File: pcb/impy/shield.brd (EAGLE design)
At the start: 137 x 101 mm, 120 parts, among them J1 USB-2410-06, J2 SI-60062-F, J3 5V, U1 AD5933YRS, U10 LTC3406AB, U11 23LCV1024-I/SN, U12 MIC2009A-1YM6, U13 ADG725BSU, U14 ADG725BSU, U15 ADG819BRT, U2 ADG704BRM, U3 AD8656ARZ, U4 M24C08WMN, U5 ADG706BRU, U6 DP83848I, U7 MIC2009A-1YM6, U8 AT25DF081A-SS, U9 SST25VF080B-80-4I-S2

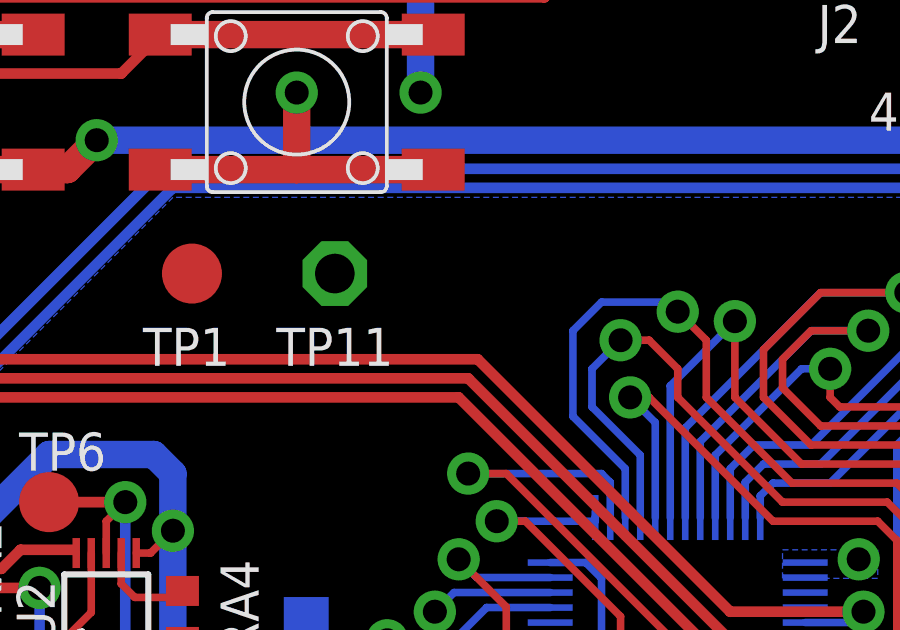
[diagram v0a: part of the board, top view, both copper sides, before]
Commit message: * pcb/impy: (shield.brd) Move GND test pin away from reset button.
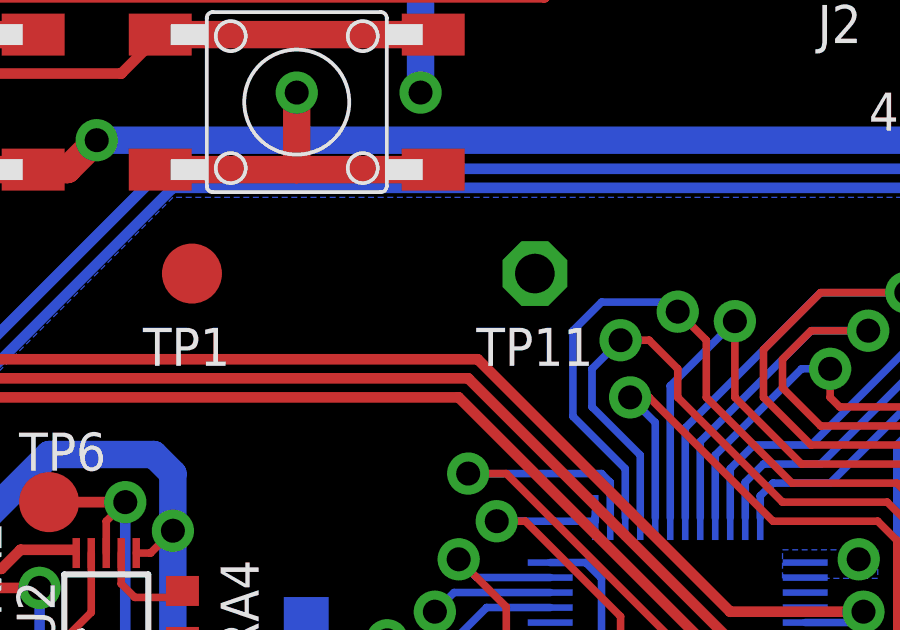
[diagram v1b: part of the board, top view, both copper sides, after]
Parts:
- moved TP11 6.67 mm to (68.6, 67.0)
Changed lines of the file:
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@@
 <attribute name="VALUE" x="47.498" y="52.0065" size="0.0254" layer="27"/>
 </element>
-<element name="TP11" library="testpad" package="P1-13" value="TPPAD1-13" x="61.9125" y="66.9925" smashed="yes">
-<attribute name="TP_SIGNAL_NAME" value="AGND" x="60.0075" y="64.135" size="1" layer="37"/>
-<attribute name="NAME" x="59.96" y="63.915" size="1.27" layer="25"/>
-<attribute name="VALUE" x="61.1505" y="65.9765" size="0.0254" layer="27"/>
+<element name="TP11" library="testpad" package="P1-13" value="TPPAD1-13" x="68.58" y="66.9925" smashed="yes">
+<attribute name="TP_SIGNAL_NAME" value="AGND" x="66.675" y="64.135" size="1" layer="37"/>
+<attribute name="NAME" x="66.6275" y="63.915" size="1.27" layer="25"/>
+<attribute name="VALUE" x="67.818" y="65.9765" size="0.0254" layer="27"/>
 </element>
 <element name="TP13" library="testpad" package="TP20R" value="TPTP20R" x="46.99" y="15.875" smashed="yes">

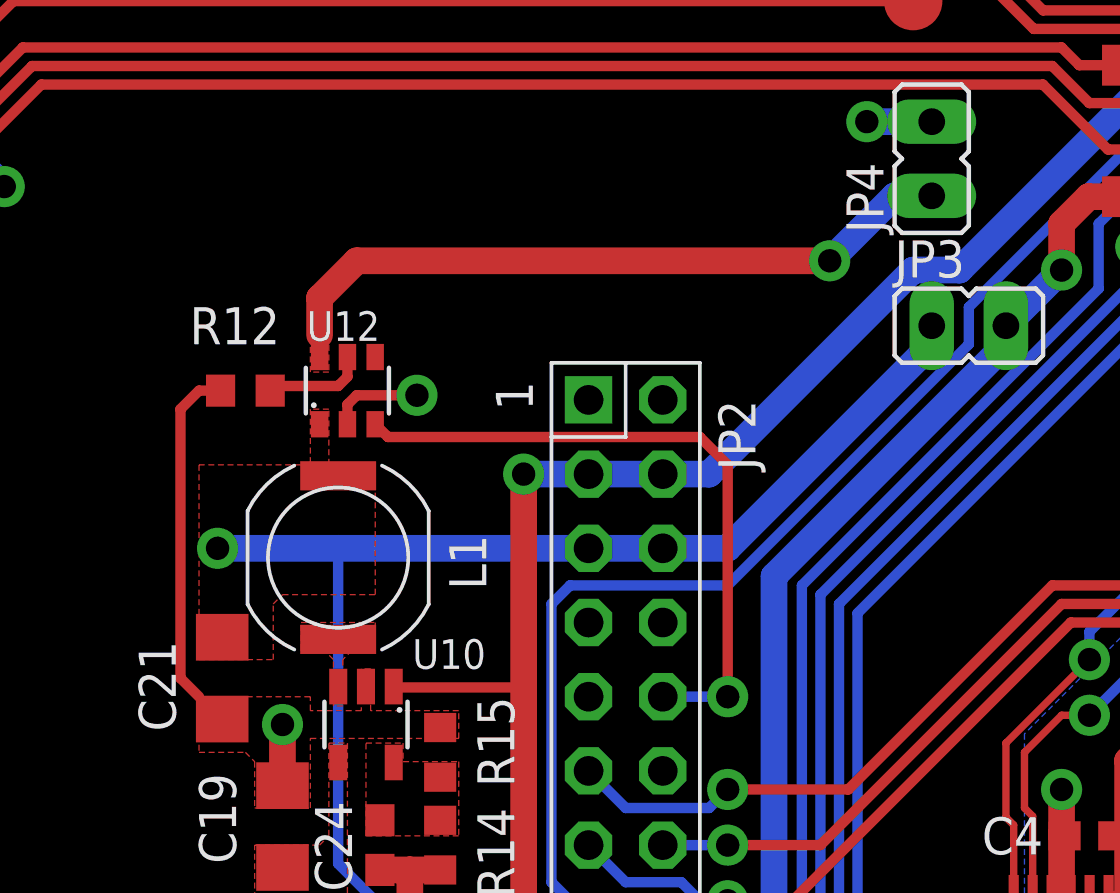
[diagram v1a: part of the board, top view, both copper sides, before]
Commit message: * pcb/impy: (shield.sch, shield.brd) Remove peripheral power switch, this doesn't really work without more effort to prevent current from flowing through STM32 pins to the peripherals. Also, it's not really needed.
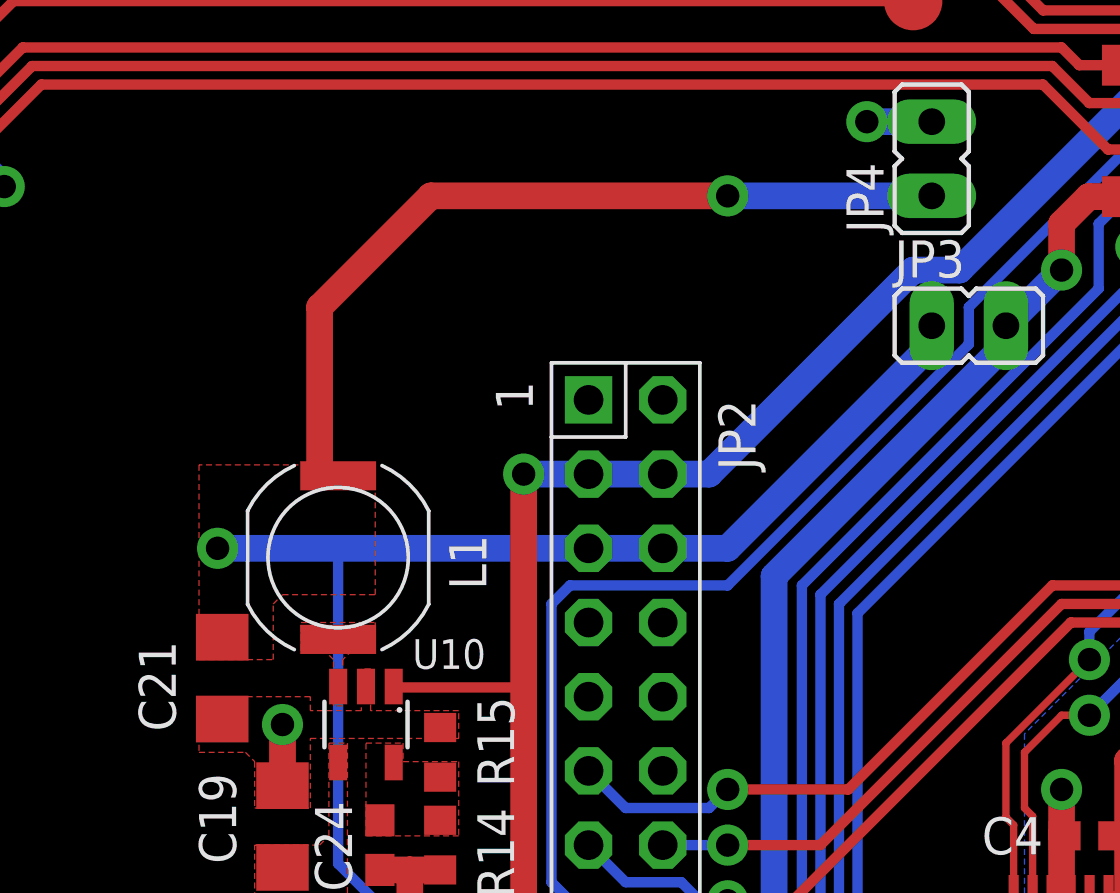
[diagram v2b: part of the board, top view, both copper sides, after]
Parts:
- removed R12: 510R, rcl:R0603
- removed U12: MIC2009A-1YM6, parts:SOT23-6
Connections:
- removed net N$36: JP4.2, U12.6
- removed net N$38: R12.2, U12.5
- removed net PC15: JP2.10, U12.3
- net +3V3: now also JP4.2; no longer U12.1
- net GND: no longer R12.1, U12.2
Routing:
- net +3V3: track 45.4 -> 73.7 mm, vias 2 -> 3
- net N$36: track 23.7 -> 0.00 mm, vias 1 -> 0
- net PC15: track 22.8 -> 0.00 mm, vias 1 -> 0
- net GND: track 115.6 -> 100.6 mm, vias 13 -> 12
- net N$38: track 3.51 -> 0.00 mm
- removed copper zone on layer 1, net N$36
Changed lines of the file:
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@@
 <attribute name="NAME" x="54.9275" y="87.2" size="1.27" layer="25" rot="R270"/>
-</element>
-<element name="U12" library="parts" package="SOT23-6" value="MIC2009A-1YM6" x="15.875" y="63.8175" smashed="yes">
-<attribute name="RS" value="727-4832" x="15.875" y="63.8175" size="1.778" layer="27" display="off"/>
-<attribute name="VALUE" x="11.6205" y="65.5905" size="1.016" layer="27" ratio="10"/>
-<attribute name="NAME" x="14.478" y="65.5195" size="1.016" layer="25" ratio="10"/>
 </element>
 <element name="D1" library="parts" package="DO214AC" value="STPS1L30A" x="30.7975" y="14.9225" smashed="yes" rot="R270">
@@
 <attribute name="NAME" x="32.401" y="16.2925" size="1.27" layer="25" ratio="10" rot="R270"/>
 <attribute name="VALUE" x="32.369" y="19.785" size="1.27" layer="27" ratio="10" rot="R270"/>
-</element>
-<element name="R12" library="rcl" package="R0603" value="510R" x="12.3825" y="63.8175" smashed="yes">
-<attribute name="NAME" x="10.4775" y="65.405" size="1.27" layer="25"/>
-<attribute name="VALUE" x="6.0325" y="63.1825" size="1.27" layer="27"/>
 </element>
 <element name="R13" library="rcl" package="R0603" value="510R" x="41.275" y="12.065" smashed="yes">
@@
 <contactref element="C23" pad="2"/>
 <contactref element="J3" pad="2"/>
-<contactref element="U12" pad="2"/>
-<contactref element="U12" pad="2"/>
-<contactref element="R12" pad="1"/>
 <contactref element="R13" pad="1"/>
 <contactref element="U10" pad="2"/>
@@
 <wire x1="10.16" y1="33.1225" x2="10.16" y2="31.4325" width="0.9144" layer="1"/>
 <via x="10.16" y="31.4325" extent="1-16" drill="0.8" shape="octagon"/>
-<wire x1="15.875" y1="62.6675" x2="15.875" y2="63.34125" width="0.3556" layer="1"/>
-<wire x1="15.875" y1="63.34125" x2="16.1925" y2="63.65875" width="0.3556" layer="1"/>
-<wire x1="11.5325" y1="63.8175" x2="10.795" y2="63.8175" width="0.3556" layer="1"/>
-<wire x1="10.795" y1="63.8175" x2="10.16" y2="63.1825" width="0.3556" layer="1"/>
-<wire x1="10.16" y1="63.1825" x2="10.16" y2="53.975" width="0.3556" layer="1"/>
-<wire x1="10.16" y1="53.975" x2="10.795" y2="53.34" width="0.3556" layer="1"/>
-<wire x1="16.1925" y1="63.65875" x2="18.25625" y2="63.65875" width="0.3556" layer="1"/>
-<via x="18.25625" y="63.65875" extent="1-16" drill="0.8" shape="octagon"/>
 <wire x1="-0.2965" y1="14.9325" x2="0.2575" y2="14.9225" width="0.3556" layer="1"/>
 <wire x1="0.2575" y1="14.9225" x2="1.5875" y2="14.9225" width="0.3556" layer="1"/>
@@
 <vertex x="16.8275" y="56.8325"/>
 <vertex x="16.8275" y="61.2775"/>
-<vertex x="15.24" y="61.2775"/>
-<vertex x="15.24" y="63.1825"/>
-<vertex x="14.605" y="63.1825"/>
-<vertex x="14.605" y="61.2775"/>
 <vertex x="10.795" y="61.2775"/>
 </polygon>
@@
 <wire x1="28.8925" y1="58.42" x2="35.8775" y2="65.405" width="0.9144" layer="16"/>
 <wire x1="35.8775" y1="65.405" x2="35.8775" y2="66.04" width="0.9144" layer="16"/>
-<contactref element="U12" pad="1"/>
 <wire x1="18.01275" y1="47.41" x2="18.01275" y2="46.27025" width="0.9144" layer="1"/>
 <wire x1="18.01275" y1="46.27025" x2="17.4625" y2="45.72" width="0.9144" layer="1"/>
@@
 <wire x1="24.13" y1="58.42" x2="15.5575" y2="58.42" width="0.9144" layer="16"/>
 <wire x1="15.5575" y1="58.42" x2="11.43" y2="58.42" width="0.9144" layer="16"/>
+<contactref element="JP4" pad="2"/>
+<via x="28.8925" y="70.485" extent="1-16" drill="0.8" shape="octagon"/>
+<wire x1="28.8925" y1="70.485" x2="18.7325" y2="70.485" width="0.9144" layer="1"/>
+<wire x1="18.7325" y1="70.485" x2="14.9225" y2="66.675" width="0.9144" layer="1"/>
+<wire x1="14.9225" y1="66.675" x2="14.9225" y2="60.96" width="0.9144" layer="1"/>
+<wire x1="35.8775" y1="70.485" x2="28.8925" y2="70.485" width="0.9144" layer="16"/>
 </signal>
 <signal name="!RST">
@@
 <wire x1="30.97" y1="12.7" x2="30.7975" y2="12.8725" width="0.9144" layer="1"/>
 </signal>
-<signal name="N$38">
-<contactref element="U12" pad="5"/>
-<contactref element="R12" pad="2"/>
-<wire x1="15.875" y1="64.9675" x2="15.875" y2="64.29375" width="0.3556" layer="1"/>
-<wire x1="15.875" y1="64.29375" x2="15.5575" y2="63.97625" width="0.3556" layer="1"/>
-<wire x1="15.5575" y1="63.97625" x2="13.39125" y2="63.97625" width="0.3556" layer="1"/>
-<wire x1="13.39125" y1="63.97625" x2="13.2325" y2="63.8175" width="0.3556" layer="1"/>
-</signal>
 <signal name="N$39">
 <contactref element="U7" pad="5"/>
@@
 <wire x1="92.329" y1="91.821" x2="89.535" y2="94.615" width="0.3556" layer="16"/>
 </signal>
-<signal name="N$36">
-<contactref element="U12" pad="6"/>
-<contactref element="JP4" pad="2"/>
-<via x="32.385" y="68.2625" extent="1-16" drill="0.8" shape="octagon"/>
-<wire x1="32.385" y1="68.2625" x2="16.1925" y2="68.2625" width="0.9144" layer="1"/>
-<wire x1="16.1925" y1="68.2625" x2="14.9225" y2="66.9925" width="0.9144" layer="1"/>
-<wire x1="14.9225" y1="66.9925" x2="14.9225" y2="65.7225" width="0.9144" layer="1"/>
-<polygon width="0.3556" layer="1" thermals="no" rank="2">
-<vertex x="15.24" y="64.4525"/>
-<vertex x="14.605" y="64.4525"/>
-<vertex x="14.605" y="66.04"/>
-<vertex x="15.24" y="66.04"/>
-</polygon>
-<wire x1="35.8775" y1="70.485" x2="34.6075" y2="70.485" width="0.9144" layer="16"/>
-<wire x1="34.6075" y1="70.485" x2="32.385" y2="68.2625" width="0.9144" layer="16"/>
-</signal>
 <signal name="PB7">
 <contactref element="JP2" pad="24"/>
@@
 <wire x1="33.02" y1="50.165" x2="40.005" y2="57.15" width="0.3556" layer="1"/>
 </signal>
-<signal name="PC15">
-<contactref element="JP2" pad="10"/>
-<contactref element="U12" pad="3"/>
-<wire x1="16.825" y1="62.6675" x2="17.2625" y2="62.23" width="0.3556" layer="1"/>
-<wire x1="17.2625" y1="62.23" x2="27.94" y2="62.23" width="0.3556" layer="1"/>
-<wire x1="27.94" y1="62.23" x2="28.8925" y2="61.2775" width="0.3556" layer="1"/>
-<wire x1="28.8925" y1="61.2775" x2="28.8925" y2="53.34" width="0.3556" layer="1"/>
-<via x="28.8925" y="53.34" extent="1-16" drill="0.8" shape="octagon"/>
-<wire x1="28.8925" y1="53.34" x2="26.67" y2="53.34" width="0.3556" layer="16"/>
-</signal>
 <signal name="PC2">

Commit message: * pcb/impy: (shield.sch) Change value of VCC/2 bypass capacitor, this can't be large because it represents a large load to the AD5933 output during coupling capacitor charging.
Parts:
- C26: value 10u -> 1n
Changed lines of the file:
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@@
 <attribute name="VALUE" x="46.6725" y="42.545" size="1.27" layer="27" rot="R90"/>
 </element>
-<element name="C26" library="rcl" package="C0603" value="10u" x="50.8" y="44.1325" smashed="yes" rot="R270">
+<element name="C26" library="rcl" package="C0603" value="1n" x="50.8" y="44.1325" smashed="yes" rot="R270">
 <attribute name="NAME" x="49.8475" y="42.38625" size="1.27" layer="25" rot="R90"/>
 <attribute name="VALUE" x="49.8475" y="42.545" size="1.27" layer="27" rot="R90"/>

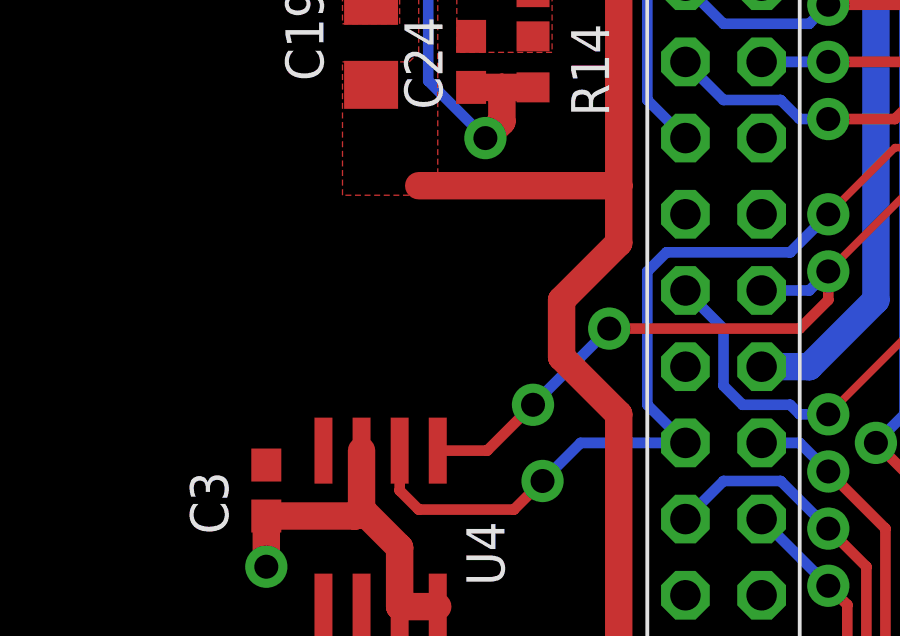
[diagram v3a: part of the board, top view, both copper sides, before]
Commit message: * pcb/impy: (shield.sch, shield.brd) Add pull up resistors to I2C clock and data lines, the ones on the discovery board are too weak for a nice 400kHz signal.
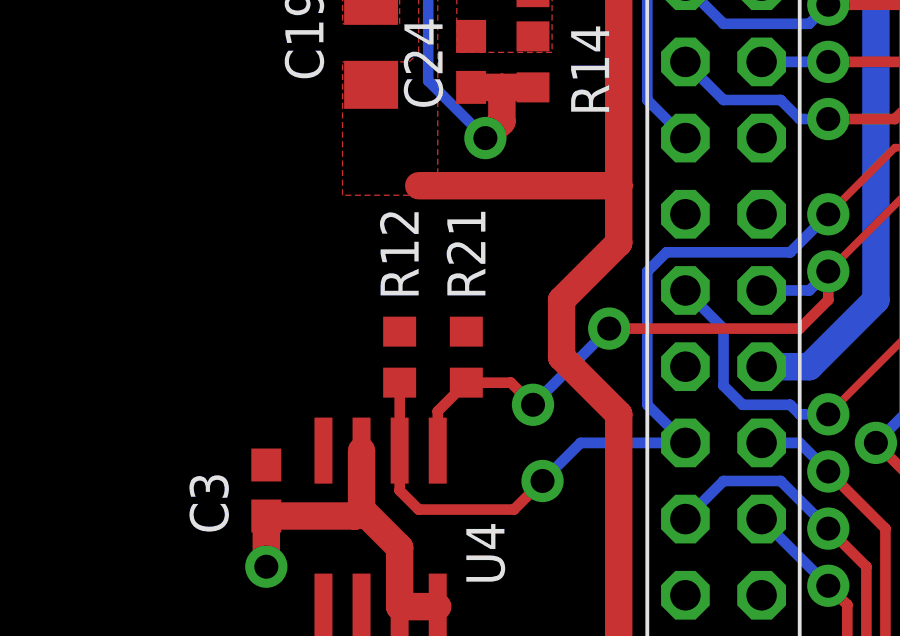
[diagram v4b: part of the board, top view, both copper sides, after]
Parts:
- added R12, R21: 3k9, rcl:R0603
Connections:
- net PB6: now also R12.1
- net PB9: now also R21.1
- net VCC: now also R12.2, R21.2
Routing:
- net PB6: track 98.3 -> 100.6 mm
- net PB9: track 95.8 -> 97.2 mm
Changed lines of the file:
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@@
 <attribute name="VALUE" x="44.7675" y="48.5775" size="1.27" layer="27" rot="R90"/>
+</element>
+<element name="R12" library="rcl" package="R0603" value="3k9" x="14.605" y="38.4175" smashed="yes" rot="R90">
+<attribute name="NAME" x="15.24" y="40.3225" size="1.27" layer="25" rot="R90"/>
+<attribute name="VALUE" x="15.24" y="40.3225" size="1.27" layer="27" rot="R90"/>
+</element>
+<element name="R21" library="rcl" package="R0603" value="3k9" x="16.8275" y="38.4175" smashed="yes" rot="R90">
+<attribute name="NAME" x="17.4625" y="40.3225" size="1.27" layer="25" rot="R90"/>
+<attribute name="VALUE" x="17.4625" y="40.3225" size="1.27" layer="27" rot="R90"/>
 </element>
 </elements>
@@
 <wire x1="21.59" y1="39.37" x2="19.05" y2="36.83" width="0.3556" layer="16"/>
 <via x="19.05" y="36.83" extent="1-16" drill="0.8" shape="octagon"/>
-<wire x1="19.05" y1="36.83" x2="17.5225" y2="35.3025" width="0.3556" layer="1"/>
-<wire x1="17.5225" y1="35.3025" x2="15.875" y2="35.3025" width="0.3556" layer="1"/>
 <wire x1="39.0525" y1="44.7675" x2="39.3325" y2="45.0475" width="0.254" layer="1"/>
 <wire x1="39.3325" y1="45.0475" x2="39.3325" y2="46.5625" width="0.254" layer="1"/>
@@
 <wire x1="39.0525" y1="51.435" x2="40.3225" y2="52.705" width="0.254" layer="1"/>
 <wire x1="40.3225" y1="52.705" x2="41.275" y2="52.705" width="0.254" layer="1"/>
+<contactref element="R21" pad="1"/>
+<wire x1="16.8275" y1="37.5675" x2="18.3125" y2="37.5675" width="0.3556" layer="1"/>
+<wire x1="18.3125" y1="37.5675" x2="19.05" y2="36.83" width="0.3556" layer="1"/>
+<wire x1="15.875" y1="35.3025" x2="15.875" y2="36.615" width="0.3556" layer="1"/>
+<wire x1="15.875" y1="36.615" x2="16.8275" y2="37.5675" width="0.3556" layer="1"/>
 </signal>
 <signal name="PB6">
@@
 <wire x1="38.6825" y1="48.9475" x2="38.4175" y2="49.2125" width="0.254" layer="1"/>
 <wire x1="41.275" y1="55.5625" x2="41.275" y2="54.61" width="0.3556" layer="16"/>
+<contactref element="R12" pad="1"/>
+<wire x1="14.605" y1="37.5675" x2="14.605" y2="35.3025" width="0.3556" layer="1"/>
 </signal>
 <signal name="USB_P">
@@
 <wire x1="46.355" y1="50.9975" x2="46.355" y2="51.435" width="0.3556" layer="1"/>
 <wire x1="46.355" y1="51.435" x2="44.60875" y2="53.18125" width="0.3556" layer="1"/>
+<contactref element="R12" pad="2"/>
+<contactref element="R21" pad="2"/>
 </signal>
 <signal name="AGND" class="1">
